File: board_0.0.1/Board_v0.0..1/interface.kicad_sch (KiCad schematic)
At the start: 1 part, among them U1 Teensy3.5

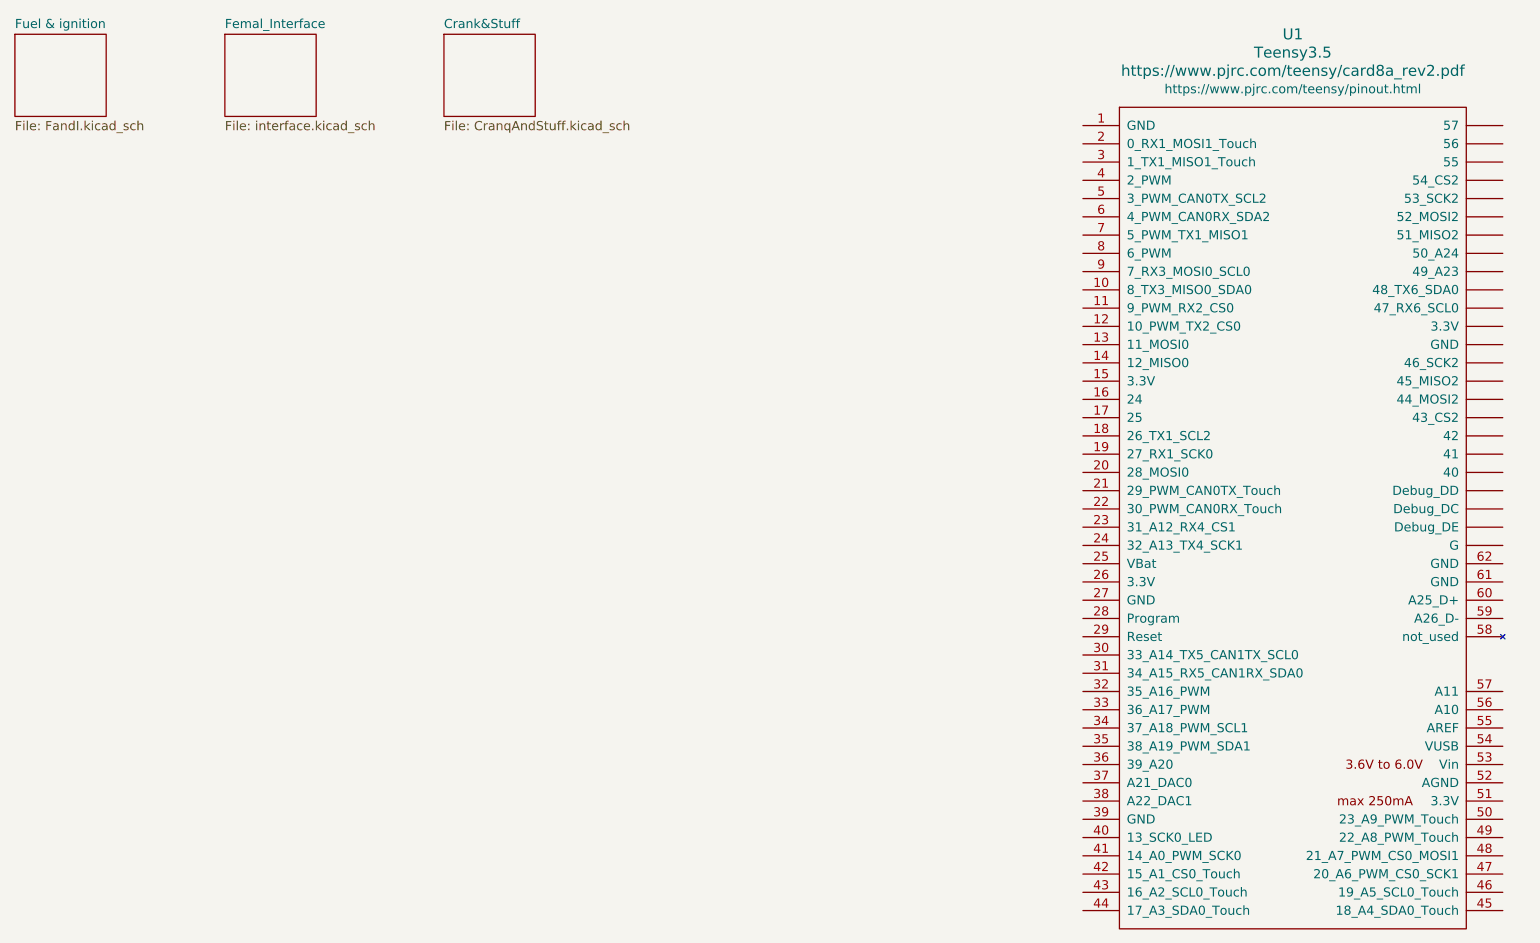
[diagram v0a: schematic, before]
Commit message: added cranq & VR conditioner, and more like iginition
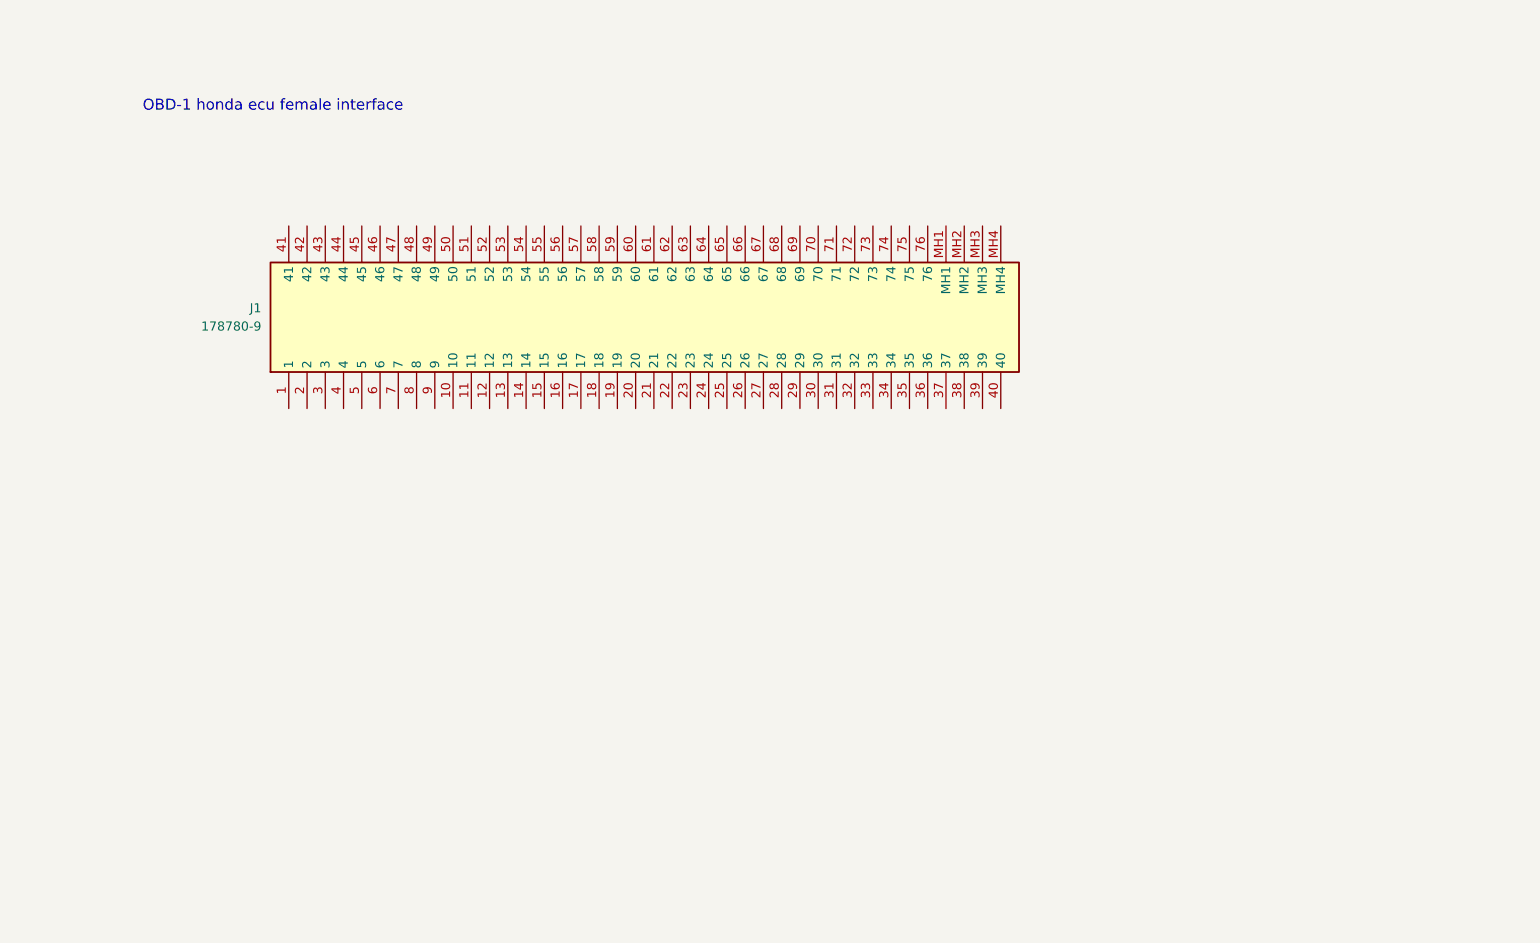
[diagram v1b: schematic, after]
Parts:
- removed U1: Teensy3.5, symbol teensy:Teensy3.5
- added J1: 178780-9, 1787809, symbol 178780-9:178780-9
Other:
- removed sheet Crank&Stuff
- removed sheet Femal_Interface
- removed sheet Fuel & ignition
- note added: "OBD-1 honda ecu female interface"
- title: honda ECU OBD-1  -> (none)
